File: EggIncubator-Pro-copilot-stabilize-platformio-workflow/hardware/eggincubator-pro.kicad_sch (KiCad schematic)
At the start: 33 parts, among them J1 ESP32 DevKit breakout, J10 ESP32 DevKit 5V / VIN input, J2 SHT31 module, I2C 0x44, J3 DS18B20, 1-Wire, J4 4 optocoupled relay-control o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, J5 BTS7960 module / motor (separ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, J6 Door and turner limit switches, J7 5V buzzer module, Q1 low-side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, J8 Expansion: I2C / ADC sensors, J9 12V DC input, Q1 PN2222A, U1 PC817, U2 PC817, U3 PC817, U4 PC817, U9 12V to 5V buck module

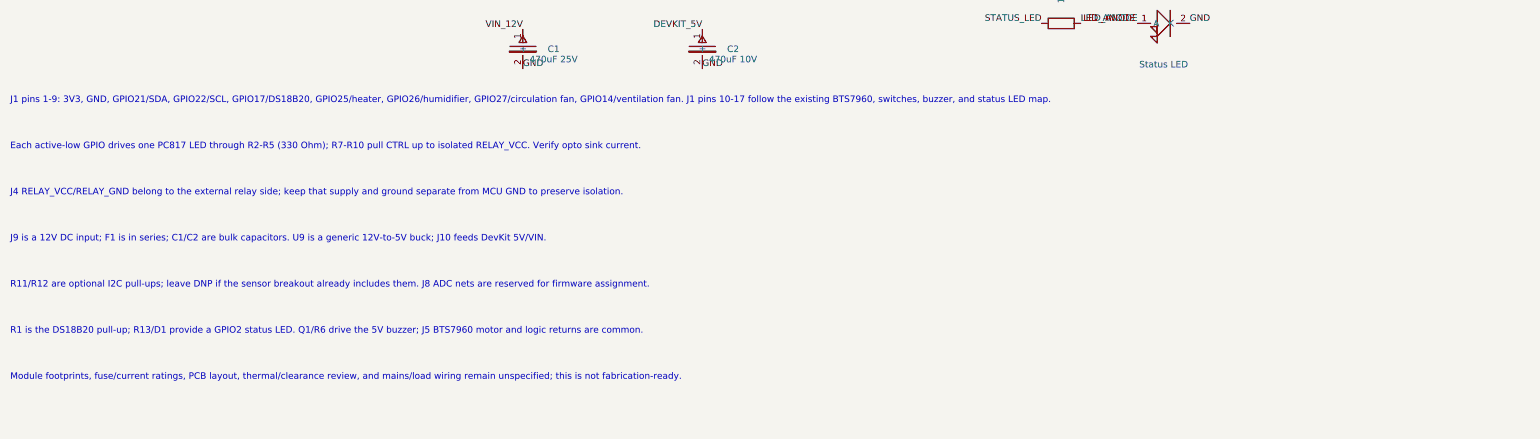
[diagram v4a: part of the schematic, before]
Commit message: Complete schematic pin map and relay notes
Co-authored-by: tomnyle <175001228+tomnyle@users.noreply.github.com>
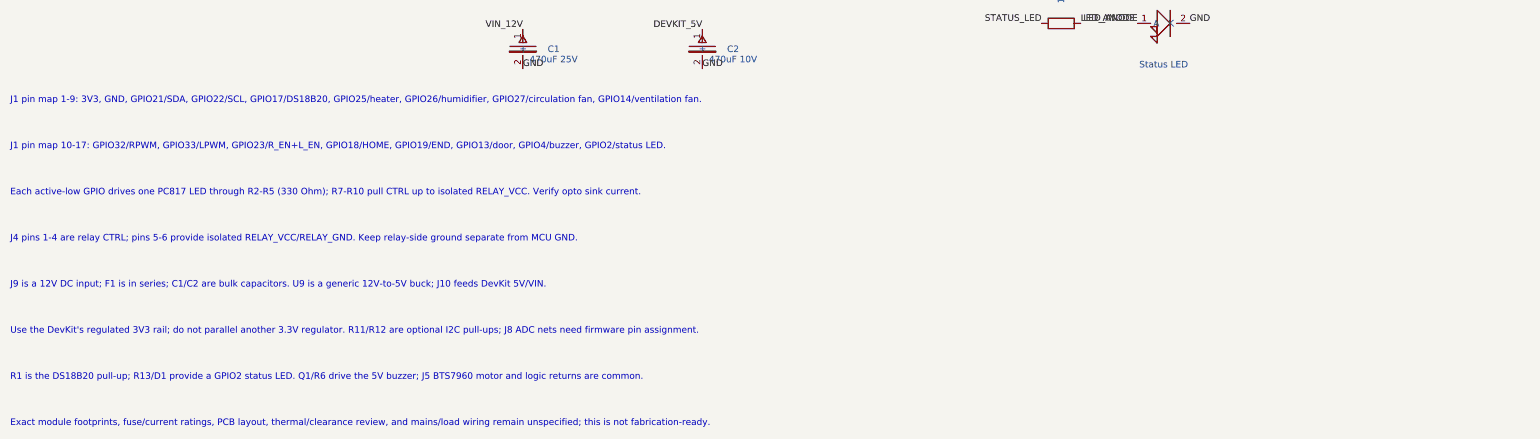
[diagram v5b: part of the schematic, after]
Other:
- note added: "Exact module footprints, fuse/current ratings, PCB layout, thermal/clearance review, and mains/load wiring remain unspecified; this is not fabrication-ready."
- note added: "J1 pin map 1-9: 3V3, GND, GPIO21/SDA, GPIO22/SCL, GPIO17/DS18B20, GPIO25/heater, GPIO26/humidifier, GPIO27/circulation fan, GPIO14/ventilation fan."
- note added: "J1 pin map 10-17: GPIO32/RPWM, GPIO33/LPWM, GPIO23/R_EN+L_EN, GPIO18/HOME, GPIO19/END, GPIO13/door, GPIO4/buzzer, GPIO2/status LED."
- note added: "J4 pins 1-4 are relay CTRL; pins 5-6 provide isolated RELAY_VCC/RELAY_GND. Keep relay-side ground separate from MCU GND."
- note added: "Use the DevKit's regulated 3V3 rail; do not parallel another 3.3V regulator. R11/R12 are optional I2C pull-ups; J8 ADC nets need firmware pin assignment."
- note removed: "J1 pins 1-9: 3V3, GND, GPIO21/SDA, GPIO22/SCL, GPIO17/DS18B20, GPIO25/heater, GPIO26/humidifier, GPIO27/circulation fan, GPIO14/ventilation fan. J1 pins 10-17 follow the existing BTS7960, switches, buzzer, and status LED map."
- note removed: "J4 RELAY_VCC/RELAY_GND belong to the external relay side; keep that supply and ground separate from MCU GND to preserve isolation."
- note removed: "Module footprints, fuse/current ratings, PCB layout, thermal/clearance review, and mains/load wiring remain unspecified; this is not fabrication-ready."
- note removed: "R11/R12 are optional I2C pull-ups; leave DNP if the sensor breakout already includes them. J8 ADC nets are reserved for firmware assignment."
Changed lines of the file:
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@@
   (label "LED_ANODE" (at 264.92 190 180) (fields_autoplaced) (effects (font (size 1.27 1.27)) (justify right bottom)))
   (label "GND" (at 275.08 190 0) (fields_autoplaced) (effects (font (size 1.27 1.27)) (justify left bottom)))
-  (text "J1 pins 1-9: 3V3, GND, GPIO21/SDA, GPIO22/SCL, GPIO17/DS18B20, GPIO25/heater, GPIO26/humidifier, GPIO27/circulation fan, GPIO14/ventilation fan. J1 pins 10-17 follow the existing BTS7960, switches, buzzer, and status LED map." (at 45 205 0) (effects (font (size 1.27 1.27)) (justify left)))
-  (text "Each active-low GPIO drives one PC817 LED through R2-R5 (330 Ohm); R7-R10 pull CTRL up to isolated RELAY_VCC. Verify opto sink current." (at 45 214 0) (effects (font (size 1.27 1.27)) (justify left)))
-  (text "J4 RELAY_VCC/RELAY_GND belong to the external relay side; keep that supply and ground separate from MCU GND to preserve isolation." (at 45 223 0) (effects (font (size 1.27 1.27)) (justify left)))
-  (text "J9 is a 12V DC input; F1 is in series; C1/C2 are bulk capacitors. U9 is a generic 12V-to-5V buck; J10 feeds DevKit 5V/VIN." (at 45 232 0) (effects (font (size 1.27 1.27)) (justify left)))
-  (text "R11/R12 are optional I2C pull-ups; leave DNP if the sensor breakout already includes them. J8 ADC nets are reserved for firmware assignment." (at 45 241 0) (effects (font (size 1.27 1.27)) (justify left)))
-  (text "R1 is the DS18B20 pull-up; R13/D1 provide a GPIO2 status LED. Q1/R6 drive the 5V buzzer; J5 BTS7960 motor and logic returns are common." (at 45 250 0) (effects (font (size 1.27 1.27)) (justify left)))
-  (text "Module footprints, fuse/current ratings, PCB layout, thermal/clearance review, and mains/load wiring remain unspecified; this is not fabrication-ready." (at 45 259 0) (effects (font (size 1.27 1.27)) (justify left)))
+  (text "J1 pin map 1-9: 3V3, GND, GPIO21/SDA, GPIO22/SCL, GPIO17/DS18B20, GPIO25/heater, GPIO26/humidifier, GPIO27/circulation fan, GPIO14/ventilation fan." (at 45 205 0) (effects (font (size 1.27 1.27)) (justify left)))
+  (text "J1 pin map 10-17: GPIO32/RPWM, GPIO33/LPWM, GPIO23/R_EN+L_EN, GPIO18/HOME, GPIO19/END, GPIO13/door, GPIO4/buzzer, GPIO2/status LED." (at 45 214 0) (effects (font (size 1.27 1.27)) (justify left)))
+  (text "Each active-low GPIO drives one PC817 LED through R2-R5 (330 Ohm); R7-R10 pull CTRL up to isolated RELAY_VCC. Verify opto sink current." (at 45 223 0) (effects (font (size 1.27 1.27)) (justify left)))
+  (text "J4 pins 1-4 are relay CTRL; pins 5-6 provide isolated RELAY_VCC/RELAY_GND. Keep relay-side ground separate from MCU GND." (at 45 232 0) (effects (font (size 1.27 1.27)) (justify left)))
+  (text "J9 is a 12V DC input; F1 is in series; C1/C2 are bulk capacitors. U9 is a generic 12V-to-5V buck; J10 feeds DevKit 5V/VIN." (at 45 241 0) (effects (font (size 1.27 1.27)) (justify left)))
+  (text "Use the DevKit's regulated 3V3 rail; do not parallel another 3.3V regulator. R11/R12 are optional I2C pull-ups; J8 ADC nets need firmware pin assignment." (at 45 250 0) (effects (font (size 1.27 1.27)) (justify left)))
+  (text "R1 is the DS18B20 pull-up; R13/D1 provide a GPIO2 status LED. Q1/R6 drive the 5V buzzer; J5 BTS7960 motor and logic returns are common." (at 45 259 0) (effects (font (size 1.27 1.27)) (justify left)))
+  (text "Exact module footprints, fuse/current ratings, PCB layout, thermal/clearance review, and mains/load wiring remain unspecified; this is not fabrication-ready." (at 45 268 0) (effects (font (size 1.27 1.27)) (justify left)))
   (sheet_instances (path "/" (page "1")))
 )
